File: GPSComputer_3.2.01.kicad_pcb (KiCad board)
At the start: 4 copper layers, 96 x 96 mm, 80 parts, among them J1 GPS_ANT_0, J2 GPS_ANT_0, J3 GPS_ANT_0, J4 2125281600, J5 Conn_02x08_Odd_Even, J6 Conn_02x08_Odd_Even, J7 GPS_ANT_0, U1 MAX-M10S-00B, U2 MAX-M10S-00B, U3 MAX-M10S-00B, U4 MAX-M10S-00B, U7 STM32F405RGTx, Y1 8MHz

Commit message: Last commit
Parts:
- added TP4: TestPoint, TestPoint:TestPoint_Pad_D1.0mm, F.Cu at (183.8, 81.3)
- C12: value 1uF -> 100nF
- C24, C28, C4, C6: value 1uF -> 10uF; footprint Capacitor_Tantalum_SMD:CP_EIA-3528-21_Kemet-B_Pad1.50x2.35mm_HandSolder -> Capacitor_SMD:C_1210_3225Metric
- D2, D4, D6, D9: value D -> B0520LW-7-F; footprint Diode_SMD:D_1206_3216Metric_Pad1.42x1.75mm_HandSolder -> B0520LW-7-F:SOD3716X145N
- moved D9 59.5 mm to (152.0, 74.3), turned to 0 degrees
- moved D4 48.8 mm to (126.9, 116.2), turned to 180 degrees
- moved D6 17.2 mm to (109.7, 116.2)
- moved C22 1.70 mm to (114.0, 119.8)
- moved C2 1.45 mm to (148.1, 119.5)
- moved C26 1.20 mm to (131.2, 119.2)
- moved C8 0.60 mm to (147.7, 71.8)
- moved C28 0.50 mm to (127.0, 126.0)
- moved C6 0.50 mm to (143.5, 126.0)
- moved J2 0.50 mm to (148.3, 50.3)
- moved J3 0.47 mm to (114.2, 141.8)
- moved J1 0.43 mm to (147.6, 141.8)
- moved J7 0.43 mm to (131.1, 141.8)
- moved C24 0.38 mm to (110.0, 126.0)
- moved D2 0.29 mm to (146.3, 112.8)
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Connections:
- D4 pad 1: Net-(D4-Pad1) -> Net-(D4-K)
- D6 pad 1: Net-(D6-Pad1) -> Net-(D6-K)
- D9 pad 1: Net-(D9-Pad1) -> Net-(D9-K)
- J4 pad 5: GPS_DBG_UART4_TX -> GPS_DBG_UART4_RX
- J4 pad 6: GPS_DBG_UART4_RX -> GPS_DBG_UART4_TX
- R17 pad 2: Net-(D6-Pad1) -> Net-(D4-K)
- R6 pad 2: Net-(D4-Pad1) -> Net-(D9-K)
- R9 pad 2: Net-(D9-Pad1) -> Net-(D6-K)
- U1 pad 7: GND -> +3.3V
- U2 pad 7: GND -> +3.3V
- U3 pad 7: GND -> +3.3V
- U4 pad 7: GND -> +3.3V
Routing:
- net GPS_DBG_UART4_TX: track 55.7 -> 58.6 mm
- net +3.3V: track 60.3 -> 63.2 mm, vias 77 -> 89
- net GPS_DBG_UART4_RX: track 64.1 -> 61.3 mm
- net GPS0_RESET: track 43.7 -> 45.7 mm
- net Net-(D4-Pad1): track 2.00 -> 0.00 mm
- net Net-(D6-Pad1): track 1.95 -> 0.00 mm
- net Net-(D9-Pad1): track 1.94 -> 0.00 mm
- net Net-(D9-K): track 0.00 -> 1.76 mm
- net Net-(D6-K): track 0.00 -> 1.74 mm
- net Net-(D4-K): track 0.00 -> 1.71 mm
- net FLI_GPS_USART1_TX: track 56.8 -> 56.1 mm
- net GPS3_RESET: track 53.0 -> 52.4 mm
- net GND: track 9.82 -> 9.29 mm, vias 492 -> 512
- net Net-(D2-K): track 2.57 -> 2.05 mm
- net Net-(J2-In): track 7.66 -> 8.16 mm

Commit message: Second commit
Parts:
- removed BT4: ML414H_IV01E, ML414H IV01E:SEIKO_ML414H_IV01E
- removed D6: B0520LW-7-F, B0520LW-7-F:SOD3716X145N
- removed D8: LED, LED_SMD:LED_0805_2012Metric_Pad1.15x1.40mm_HandSolder
- removed J7: GPS_ANT_0, Connector_Coaxial:SMA_Samtec_SMA-J-P-X-ST-EM1_EdgeMount
- removed JP1: SJumper, Jumper:SolderJumper-2_P1.3mm_Open_TrianglePad1.0x1.5mm
- removed L4: 27nH, Inductor_SMD:L_0402_1005Metric
- removed U4: MAX-M10S-00B, MAX-M10S-00B:MAXM10S00B
- added C23: 1uF, Capacitor_SMD:C_1210_3225Metric, F.Cu at (110.5, 122.0)
- added C27: 100n, Capacitor_SMD:C_0402_1005Metric, F.Cu at (159.8, 112.5)
- added C3: 1uF, Capacitor_SMD:C_1210_3225Metric, F.Cu at (157.2, 69.1)
- added C5: 10uF, Capacitor_SMD:C_1210_3225Metric, F.Cu at (160.4, 69.1)
- added IC1: 24AA32A-I_ST, 24AA32A-I_ST:SOP65P640X120-8N, F.Cu at (141.0, 75.9)
- added IC2: 24AA32A-I_ST, 24AA32A-I_ST:SOP65P640X120-8N, F.Cu at (128.4, 114.8)
- added IC3: 24AA32A-I_ST, 24AA32A-I_ST:SOP65P640X120-8N, F.Cu at (156.4, 114.8)
- added R18: 10K, Resistor_SMD:R_0402_1005Metric, F.Cu at (110.8, 131.0)
- added R19: 4.7K, Resistor_SMD:R_0402_1005Metric, F.Cu at (130.8, 111.3)
- added R20: 4.7K, Resistor_SMD:R_0402_1005Metric, F.Cu at (128.8, 109.5)
- added R21: 10K, Resistor_SMD:R_0402_1005Metric, F.Cu at (138.7, 131.0)
- added R22: 4.7K, Resistor_SMD:R_0402_1005Metric, F.Cu at (159.8, 117.2)
- added R23: 4.7K, Resistor_SMD:R_0402_1005Metric, F.Cu at (161.7, 115.1)
- added U5: SN74LV4052APWR, SN74LV4052APWR:PW16, F.Cu at (123.0, 79.8)
- BT1, BT2, BT3, R11: moved to B.Cu
- C1, C9: value 10nF -> 1.0 uF; footprint Capacitor_SMD:C_0402_1005Metric -> Capacitor_SMD:C_0805_2012Metric
- C2, C22: value 1.0 uF -> 100nF; footprint Capacitor_SMD:C_0805_2012Metric -> Capacitor_SMD:C_0402_1005Metric
- C25: value 10nF -> 100n
- C26: value 1.0 uF -> 10uF; footprint Capacitor_SMD:C_0805_2012Metric -> Capacitor_SMD:C_1210_3225Metric
- C28: value 10uF -> 1uF; footprint Capacitor_SMD:C_1210_3225Metric -> Capacitor_SMD:C_0402_1005Metric
- C4: value 10uF -> 100n; footprint Capacitor_SMD:C_1210_3225Metric -> Capacitor_SMD:C_0402_1005Metric
- C6: value 10uF -> 1uF
- C7: value 10nF -> 100nF
- D1: value LED -> B0520LW-7-F; footprint LED_SMD:LED_0805_2012Metric_Pad1.15x1.40mm_HandSolder -> B0520LW-7-F:SOD3716X145N
- D2: value B0520LW-7-F -> LED; footprint B0520LW-7-F:SOD3716X145N -> LED_SMD:LED_0805_2012Metric_Pad1.15x1.40mm_HandSolder
- J1, J2, J3: footprint Connector_Coaxial:SMA_Samtec_SMA-J-P-X-ST-EM1_EdgeMount -> Connector_Coaxial:SMA_Samtec_SMA-J-P-H-ST-EM1_EdgeMount
- R1, R15: value 10R -> 1K; footprint Resistor_SMD:R_0402_1005Metric -> Resistor_SMD:R_0805_2012Metric
- R16, R2: value 1K -> 10R; footprint Resistor_SMD:R_0805_2012Metric -> Resistor_SMD:R_0402_1005Metric
- R7: value 10R -> 10K
- R8, R9: value 1K -> 4.7K; footprint Resistor_SMD:R_0805_2012Metric -> Resistor_SMD:R_0402_1005Metric
- U1, U2, U3: value MAX-M10S-00B -> NEO-M9N; footprint MAX-M10S-00B:MAXM10S00B -> NEO-M9N:XCVR_NEO-M9N
- moved R7 86.6 mm to (156.6, 59.9)
- moved U3 71.6 mm to (147.1, 63.8), turned to -90 degrees
- moved U2 68.5 mm to (120.6, 127.0), turned to 90 degrees
- moved R8 50.3 mm to (137.5, 73.5), turned to 0 degrees
- moved C28 49.1 mm to (127.7, 77.0)
- moved R9 46.0 mm to (135.8, 75.6), turned to 0 degrees
- moved D5 30.8 mm to (106.9, 128.4), turned to 0 degrees
- moved R15 29.9 mm to (114.2, 114.3), turned to 180 degrees
- moved C25 27.7 mm to (126.1, 111.3), turned to 90 degrees
- moved R17 24.2 mm to (110.5, 128.4), turned to 0 degrees
- moved R1 23.7 mm to (141.9, 114.8), turned to 180 degrees
- moved C1 22.8 mm to (141.8, 116.7), turned to 180 degrees
- moved C9 21.8 mm to (114.2, 116.2), turned to 180 degrees
- moved D3 20.7 mm to (160.7, 62.3), turned to 180 degrees
- moved C22 20.6 mm to (124.1, 137.8)
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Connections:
- C1 pad 1: Net-(C1-Pad1) -> GPS2_V_BCKP
- C2 pad 1: GPS2_V_BCKP -> Net-(C2-Pad1)
- C22 pad 1: GPS3_V_BCKP -> Net-(C22-Pad1)
- C25 pad 1: Net-(C25-Pad1) -> +3.3V
- C26 pad 1: GPS1_V_BCKP -> +3.3V
- C9 pad 1: Net-(C9-Pad1) -> GPS1_V_BCKP
- D1 pad 1: GND -> Net-(D1-K)
- D1 pad 2: Net-(D1-A) -> +3.3V
- D2 pad 1: Net-(D2-K) -> GND
- D2 pad 2: +3.3V -> Net-(D2-A)
- J4 pad 10: unconnected-(J4-Pad10) -> GPS_MUX_UART_RX
- J4 pad 11: unconnected-(J4-Pad11) -> GPS_MUX_UART_TX
- L1 pad 1: Net-(C1-Pad1) -> Net-(C2-Pad1)
- L3 pad 1: Net-(C25-Pad1) -> Net-(C22-Pad1)
- L3 pad 2: Net-(J7-In) -> Net-(J3-In)
- R1 pad 1: Net-(C1-Pad1) -> GPS2_V_BCKP
- R1 pad 2: Net-(U1-VCC_RF) -> Net-(D1-K)
- R15 pad 1: Net-(C25-Pad1) -> GPS1_V_BCKP
- R15 pad 2: Net-(U4-VCC_RF) -> Net-(D4-K)
- R16 pad 1: Net-(D5-A) -> Net-(C22-Pad1)
- R16 pad 2: GPS1_TIMEPULSE -> GPS1_RF
- R17 pad 1: GPS1_V_BCKP -> Net-(D5-A)
- R17 pad 2: Net-(D4-K) -> GPS1_TIMEPULSE
- R2 pad 1: Net-(D1-A) -> Net-(C2-Pad1)
- R2 pad 2: GPS2_TIMEPULSE -> GPS2_RF
- R3 pad 1: GPS2_V_BCKP -> Net-(D2-A)
- R3 pad 2: Net-(D2-K) -> GPS2_TIMEPULSE
- R4 pad 2: Net-(U2-VCC_RF) -> GPS0_RF
- R7 pad 1: Net-(C9-Pad1) -> GPS0_D_SEL
- R7 pad 2: Net-(U3-VCC_RF) -> +3.3V
- R8 pad 1: Net-(D8-A) -> +3.3V
- R8 pad 2: GPS3_TIMEPULSE -> GPS0_I2C_SDA
- R9 pad 1: GPS3_V_BCKP -> +3.3V
- R9 pad 2: Net-(D6-K) -> GPS0_I2C_SCL
- U1 pad 1: GND -> unconnected-(U1-SAFEBOOT_N-Pad1)
- U1 pad 13: unconnected-(U1-LNA_EN-Pad13) -> GND
- U1 pad 14: Net-(U1-VCC_RF) -> unconnected-(U1-LNA_EN-Pad14)
- U1 pad 18: unconnected-(U1-SAFEBOOT_N-Pad18) -> GPS2_I2C_SDA
- U1 pad 2: GPS2_USART6_RX -> GPS2_D_SEL
- U1 pad 3: GPS2_USART6_TX -> GPS2_TIMEPULSE
- U1 pad 4: GPS2_TIMEPULSE -> unconnected-(U1-EXTINT-Pad4)
- U1 pad 6: GPS2_V_BCKP -> unconnected-(U1-USB_DP-Pad6)
- U1 pad 7: +3.3V -> unconnected-(U1-V_USB-Pad7)
- U1 pad 8: +3.3V -> GPS2_RESET
- U1 pad 9: GPS2_RESET -> GPS2_RF
- U2 pad 1: GND -> unconnected-(U2-SAFEBOOT_N-Pad1)
- U2 pad 11: Net-(J2-In) -> Net-(J3-In)
- U2 pad 13: unconnected-(U2-LNA_EN-Pad13) -> GND
- U2 pad 14: Net-(U2-VCC_RF) -> unconnected-(U2-LNA_EN-Pad14)
- U2 pad 18: unconnected-(U2-SAFEBOOT_N-Pad18) -> GPS1_I2C_SDA
- U2 pad 2: GPS0_UART5_RX -> GPS1_D_SEL
- U2 pad 3: GPS0_UART5_TX -> GPS1_TIMEPULSE
- U2 pad 4: GPS0_TIMEPULSE -> unconnected-(U2-EXTINT-Pad4)
- U2 pad 6: GPS0_V_BCKP -> unconnected-(U2-USB_DP-Pad6)
- U2 pad 7: +3.3V -> unconnected-(U2-V_USB-Pad7)
- U2 pad 8: +3.3V -> GPS1_RESET
- U2 pad 9: GPS0_RESET -> GPS1_RF
- U3 pad 1: GND -> unconnected-(U3-SAFEBOOT_N-Pad1)
- U3 pad 11: Net-(J3-In) -> Net-(J2-In)
- U3 pad 13: unconnected-(U3-LNA_EN-Pad13) -> GND
- U3 pad 14: Net-(U3-VCC_RF) -> unconnected-(U3-LNA_EN-Pad14)
- U3 pad 18: unconnected-(U3-SAFEBOOT_N-Pad18) -> GPS0_I2C_SDA
- U3 pad 2: GPS3_USART2_RX -> GPS0_D_SEL
- U3 pad 3: GPS3_USART2_TX -> GPS0_TIMEPULSE
- U3 pad 4: GPS3_TIMEPULSE -> unconnected-(U3-EXTINT-Pad4)
- U3 pad 6: GPS3_V_BCKP -> unconnected-(U3-USB_DP-Pad6)
- U3 pad 7: +3.3V -> unconnected-(U3-V_USB-Pad7)
- U3 pad 8: +3.3V -> GPS0_RESET
- U3 pad 9: GPS3_RESET -> GPS0_RF
- U7 pad 15: GPS3_RESET -> unconnected-(U7-PA1-Pad15)
- U7 pad 16: GPS3_USART2_TX -> GPS1_USART2_TX
- U7 pad 17: GPS3_USART2_RX -> GPS1_USART2_RX
- U7 pad 23: GPS1_RESET -> unconnected-(U7-PA7-Pad23)
- U7 pad 26: unconnected-(U7-PB0-Pad26) -> GPS1_RESET
- U7 pad 29: GPS1_USART3_TX -> unconnected-(U7-PB10-Pad29)
- U7 pad 30: GPS1_USART3_RX -> unconnected-(U7-PB11-Pad30)
- U7 pad 34: GPS2_RESET -> unconnected-(U7-PB13-Pad34)
- U7 pad 39: unconnected-(U7-PC8-Pad39) -> GPS2_RESET
- U7 pad 55: GPS0_RESET -> unconnected-(U7-PB3-Pad55)
- U7 pad 57: unconnected-(U7-PB5-Pad57) -> GPS0_RESET
- U7 pad 59: unconnected-(U7-PB7-Pad59) -> GPS_MUX_A
- U7 pad 61: unconnected-(U7-PB8-Pad61) -> GPS_MUX_B
- U7 pad 62: unconnected-(U7-PB9-Pad62) -> GPS_MUX_INH
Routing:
- net GPS_MUX_UART_TX: track 0.00 -> 84.7 mm, vias 0 -> 1
- net GPS1_USART2_RX: track 0.00 -> 78.2 mm, vias 0 -> 2
- net GPS_MUX_UART_RX: track 0.00 -> 68.0 mm, vias 0 -> 1
- net GPS1_USART2_TX: track 0.00 -> 62.8 mm
- net GPS3_RESET: track 52.4 -> 0.00 mm
- net GPS2_USART6_TX: track 37.4 -> 79.1 mm, vias 0 -> 2
- net GPS0_UART5_TX: track 22.5 -> 59.6 mm, vias 0 -> 2
- net GPS2_USART6_RX: track 39.9 -> 76.5 mm, vias 0 -> 2
- net GPS3_USART2_TX: track 32.3 -> 0.00 mm
- net GPS_MUX_INH: track 0.00 -> 31.6 mm
- net GPS3_USART2_RX: track 31.5 -> 0.00 mm
- net GPS2_RESET: track 32.0 -> 62.6 mm
- net GPS0_UART5_RX: track 22.9 -> 52.7 mm, vias 0 -> 2
- net GPS1_USART3_TX: track 25.9 -> 0.00 mm
- net GPS1_USART3_RX: track 25.6 -> 0.00 mm
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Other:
- outline, holes or cut-outs redrawn

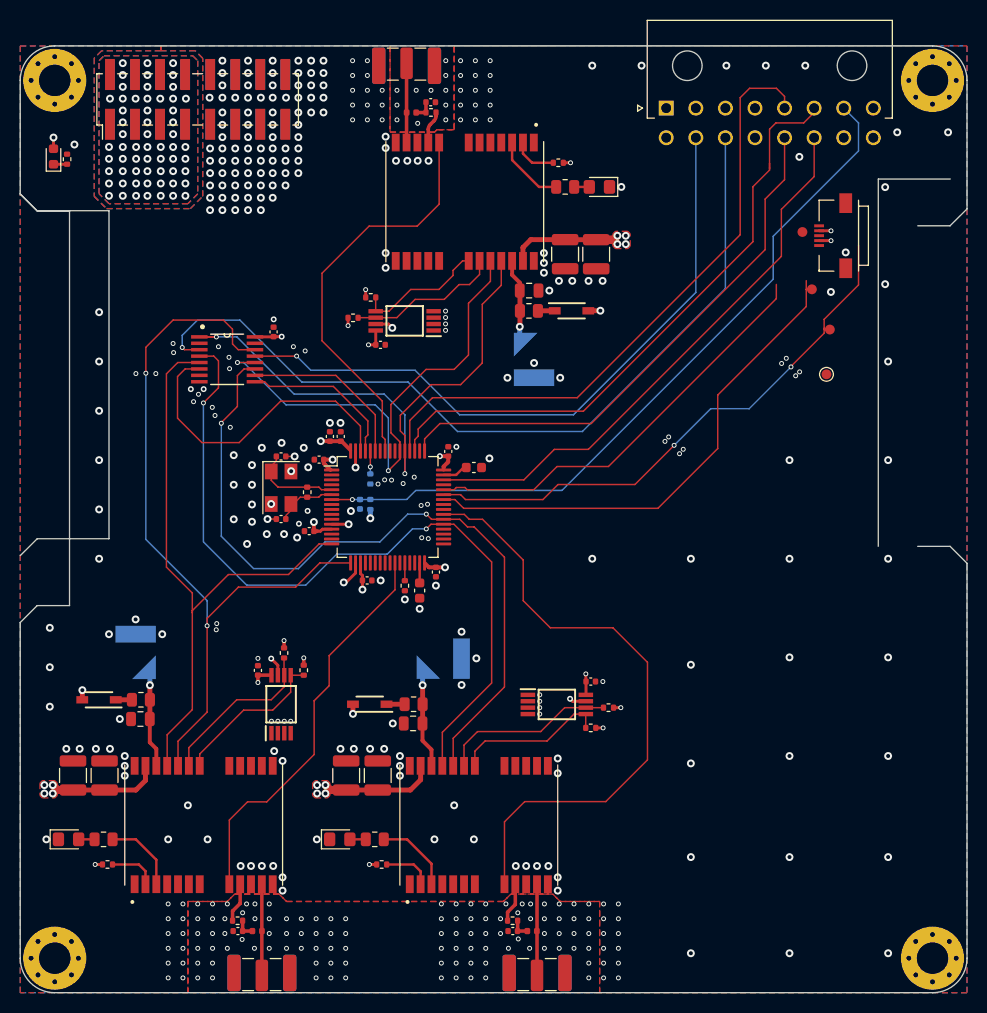
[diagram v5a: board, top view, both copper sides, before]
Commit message: Correcet MUX pins
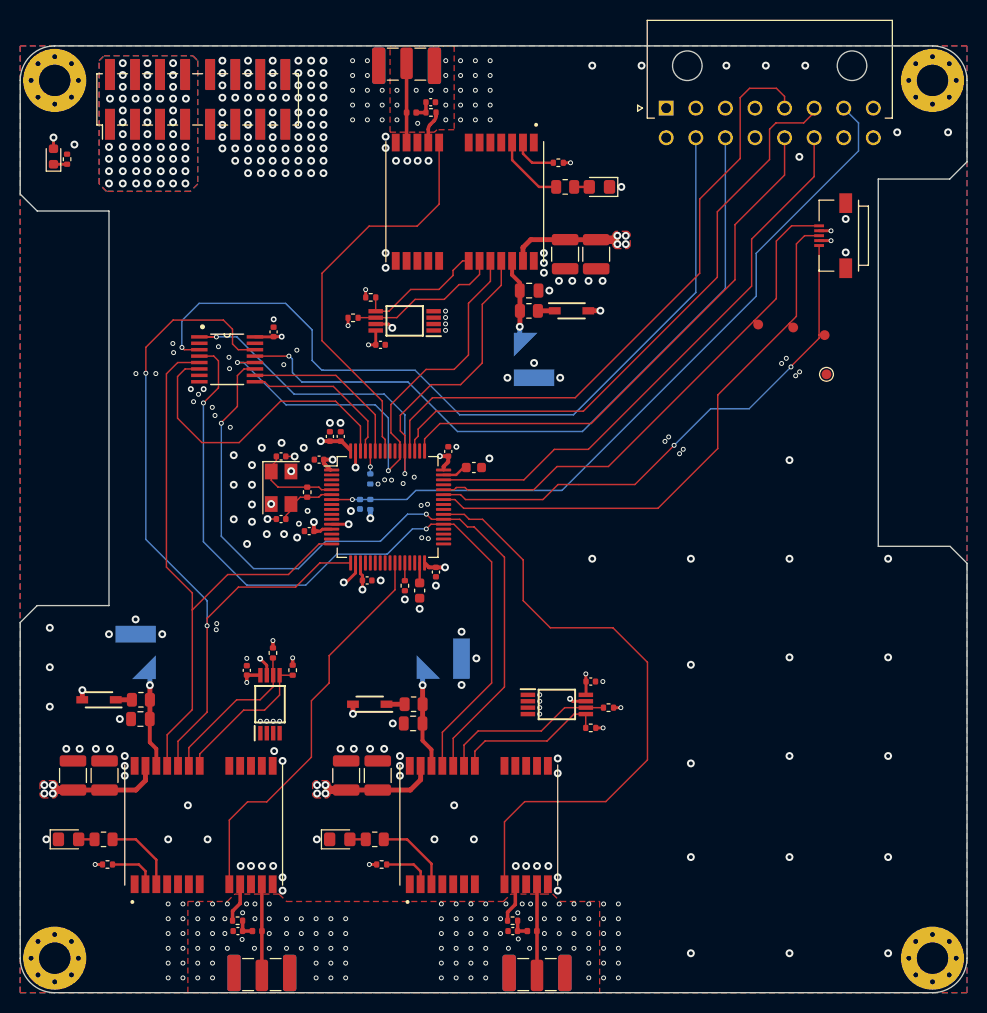
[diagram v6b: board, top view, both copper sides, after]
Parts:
- moved TP3 10.4 mm to (176.8, 76.2)
- moved TP1 4.31 mm to (180.4, 76.5)
- moved C25 1.12 mm to (125.0, 111.3)
- moved R19 1.12 mm to (129.6, 111.3)
- moved R20 1.12 mm to (127.6, 109.5)
- moved IC2 1.12 mm to (127.3, 114.8)
- moved TP2 0.77 mm to (183.6, 77.3)
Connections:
- U5 pad 13: GPS_MUX_UART_RX -> GPS_MUX_UART_TX
- U5 pad 3: GPS_MUX_UART_TX -> GPS_MUX_UART_RX
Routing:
- net GPS_MUX_UART_RX: track 68.0 -> 84.7 mm
- net GPS_MUX_UART_TX: track 84.7 -> 73.0 mm
- net FLI_GPS_USART1_CTS: track 43.4 -> 53.3 mm
- net FLI_GPS_USART1_TX: track 52.0 -> 57.9 mm
- net FLI_GPS_USART1_RX: track 56.8 -> 55.0 mm
- net GPS1_I2C_SCL: track 17.0 -> 15.9 mm
- net GPS1_I2C_SDA: track 16.1 -> 15.1 mm
- net GPS_DBG_UART4_TX: track 62.5 -> 61.9 mm
- net GND: vias 441 -> 416
- net +3.3V: vias 96 -> 89
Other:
- outline, holes or cut-outs redrawn
